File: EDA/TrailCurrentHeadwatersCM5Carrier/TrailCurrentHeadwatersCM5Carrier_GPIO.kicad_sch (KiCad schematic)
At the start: 29 parts, among them J14 JST_SHBM04B-SRSS-TB, J2 Conn_02x07_Odd_Even, J3 Conn_01x03, J7 Micro_SD_Card_Det, J8 THD-20-R, J9 THD-02-R, SW1 Right angle Tact button, U1 TPD4EUSB30, U18 RT9742GGJ5, U2 TPD4EUSB30, U3 MagJack-A70-112-331N126

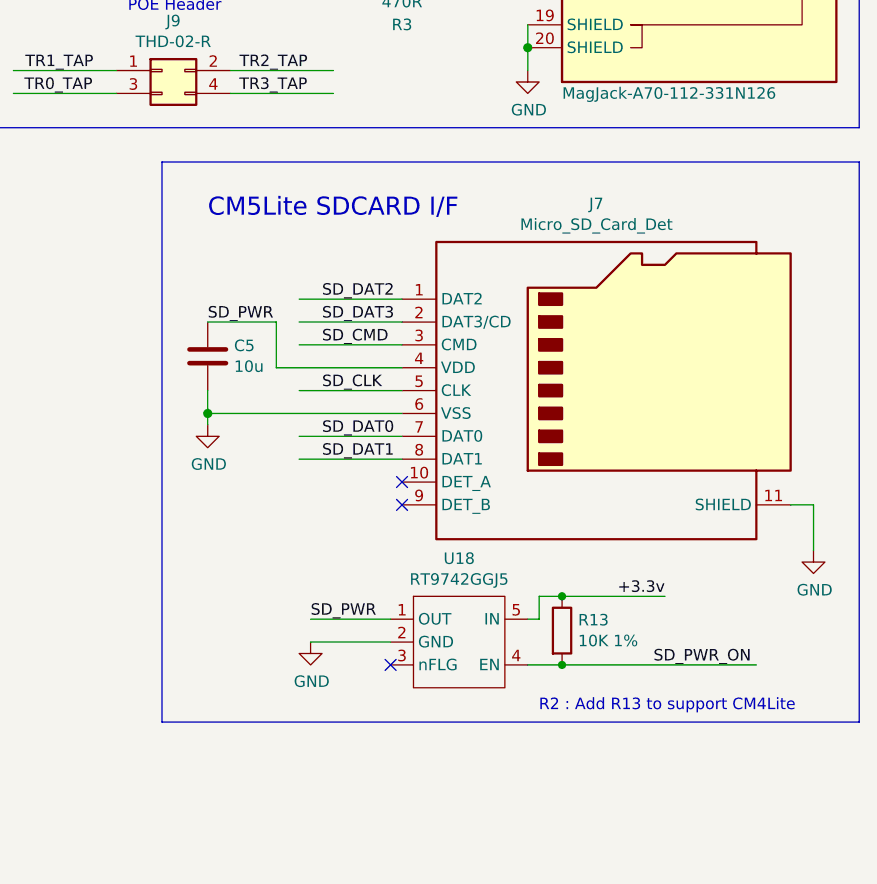
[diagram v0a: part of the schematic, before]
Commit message: Carrier board updated to point to items brought into our own libraries
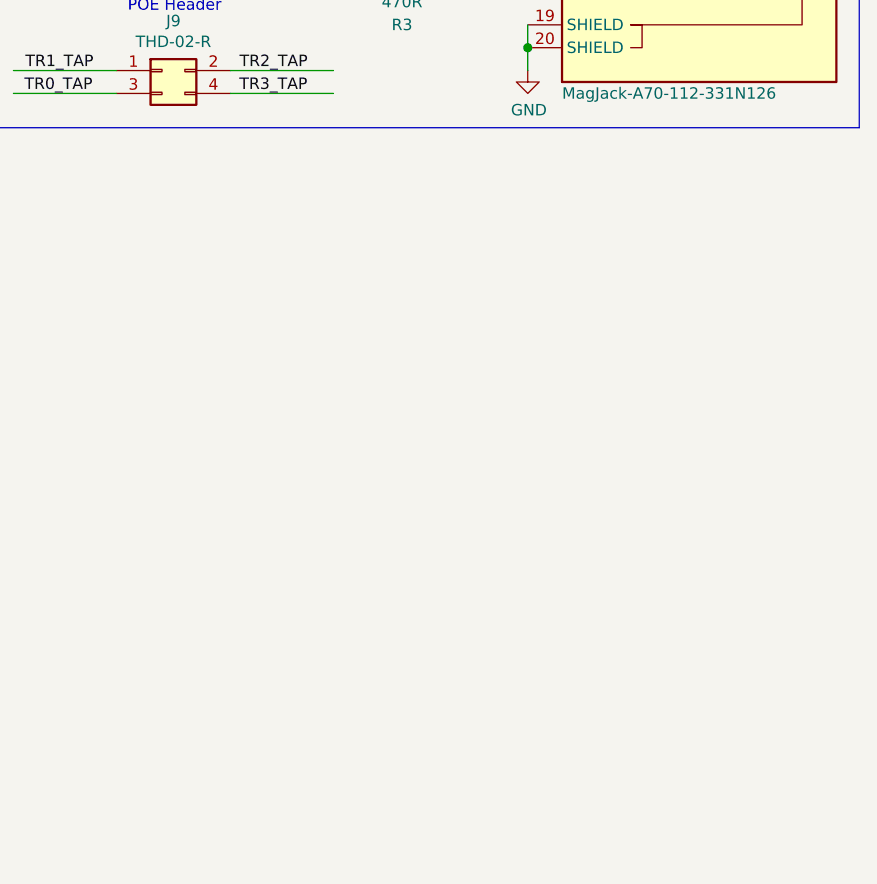
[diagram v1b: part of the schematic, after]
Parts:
- removed C5: 10u, Capacitor_SMD:C_0805_2012Metric, symbol Device:C
- removed J7: Micro_SD_Card_Det, TrailCurrentHeadwatersCM5Carrier:SDCARD_MOLEX_503398-1892, symbol Connector:Micro_SD_Card_Det2
- removed R13: 10K 1%, Resistor_SMD:R_0402_1005Metric, symbol Device:R
- removed U18: RT9742GGJ5, Package_TO_SOT_SMD:SOT-23-5, symbol TrailCurrentHeadwatersCM5Carrier:RT9742GGJ5
- BT1: footprint TrailCurrentHeadwatersCM5Carrier:BatteryHolder_Keystone_3034_1x20mm -> TrailCurrentFootprints:BatteryHolder_Keystone_3034_1x20mm
- Module1: footprint TrailCurrentHeadwatersCM5Carrier:Raspberry-Pi-5-Compute-Module -> TrailCurrentFootprints:Raspberry-Pi-5-Compute-Module; symbol TrailCurrentHeadwatersCM5Carrier:ComputeModule5-CM5 -> TrailCurrentSymbolLibrary:ComputeModule5-CM5
- U1, U2: symbol TrailCurrentHeadwatersCM5Carrier:TPD4EUSB30 -> TrailCurrentSymbolLibrary:TPD4EUSB30
- U3: footprint TrailCurrentHeadwatersCM5Carrier:TRJG0926HENL -> TrailCurrentFootprints:TRJG0926HENL; symbol TrailCurrentHeadwatersCM5Carrier:MagJack-A70-112-331N126 -> TrailCurrentSymbolLibrary:MagJack-A70-112-331N126
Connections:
- no-connect marks 9 -> 6
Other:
- note removed: "CM5Lite SDCARD I/F"
- note removed: "R2 : Add R13 to support CM4Lite"
